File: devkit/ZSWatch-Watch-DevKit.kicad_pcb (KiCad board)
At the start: 4 copper layers, 100 x 70 mm, 132 parts, among them IC401 nPM1300-QEXX, IC501 APDS-9306-065, IC502 BMI270, IC503 LIS2MDLTR, IC504 BMP581, IC505 DRV2603RUNT, IC506 PCA9306JK, IC507 RV-8263-C8, IC601 FAN5622SX, IC602 USBLC6-2P6, IC603 MX25U51245GZ4I00, IC604 NTS0104GU12, M601 NORA-B106, Q401 PMZ550UNEYL, Q402 PMZ550UNEYL, Q403 PMZ550UNEYL, Q404 PMZB320UPEYL, X401 Battery, X402 Battery, X403 Power, X404 VSYS, X501 Current, X502 I2S, X503 Current, X504 I2C, X505 Current, X506 Current, X507 Current, X508 Current, X509 Motor, X510 Current, X601 DEBUG, X602 Current, X603 Device, X604 UART, X605 GPIO, X606 Current, X607 IO Current, X608 Display, X609 Display, X610 LED Current

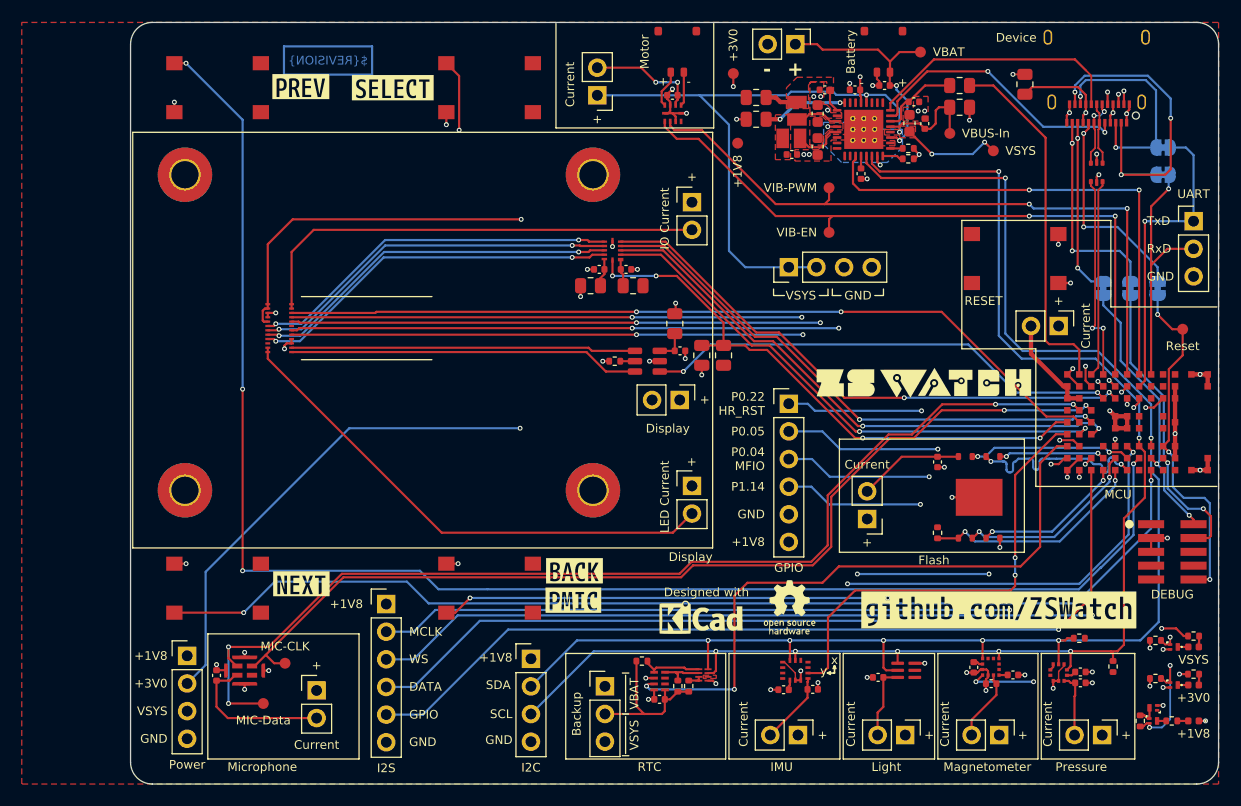
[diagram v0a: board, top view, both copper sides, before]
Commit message: Bug: Issue #198
- Change 3V0 to 3V3 to prevent flickering display

Closes: #198

Signed-off-by: Daniel Kampert <DanielKampert@kampis-elektroecke.de>
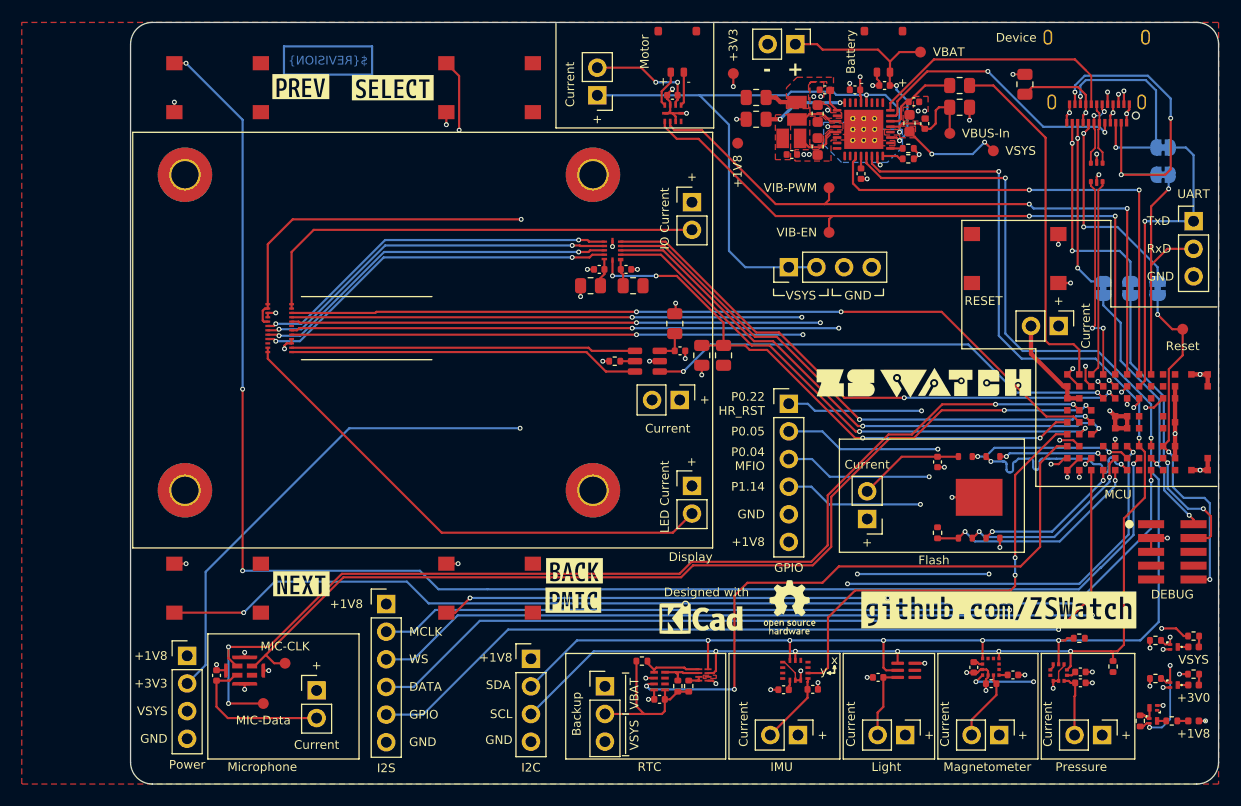
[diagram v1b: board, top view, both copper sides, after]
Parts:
- TP405: value +3V0 -> +3V3
- X609: value Display -> Current
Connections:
- net +3V0 renamed +3V3
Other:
- board text added: "+3V3"
- board text removed: "+3V0"
